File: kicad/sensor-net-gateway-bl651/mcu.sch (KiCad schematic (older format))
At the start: 14 parts

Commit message: added power and usb2uart
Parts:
- gave numbers to parts that had none: 14
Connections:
- net FTDI_DIO0: now reaches BL1.12 (P0.12)
- net FTDI_DIO1: now reaches BL1.13 (P0.11)
- net FTDI_DIO2: now reaches BL1.14 (P0.10)
- net FTDI_DIO3: now reaches BL1.15 (P0.09)
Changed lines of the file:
@@
 $EndDescr
 $Comp
-L HH_Laird:BL651 BL?
+L HH_Laird:BL651 BL1
 U 1 1 5F8C7148
 P 5700 2900
-F 0 "BL?" H 5700 3915 50  0000 C CNN
+F 0 "BL1" H 5700 3915 50  0000 C CNN
 F 1 "BL651" H 5700 3824 50  0000 C CNN
 F 2 "HH_Laird:BL651" V 4900 3300 50  0001 C CNN
@@
 $EndComp
 $Comp
-L power:GND #PWR?
+L power:GND #PWR0101
 U 1 1 5F8C844D
 P 7250 2250
-F 0 "#PWR?" H 7250 2000 50  0001 C CNN
+F 0 "#PWR0101" H 7250 2000 50  0001 C CNN
 F 1 "GND" H 7255 2077 50  0000 C CNN
 F 2 "" H 7250 2250 50  0001 C CNN
@@
 $EndComp
 $Comp
-L power:GND #PWR?
+L power:GND #PWR0102
 U 1 1 5F8C8B4E
 P 4100 2650
-F 0 "#PWR?" H 4100 2400 50  0001 C CNN
+F 0 "#PWR0102" H 4100 2400 50  0001 C CNN
 F 1 "GND" H 4105 2477 50  0000 C CNN
 F 2 "" H 4100 2650 50  0001 C CNN
@@
 $EndComp
 $Comp
-L power:GND #PWR?
+L power:GND #PWR0103
 U 1 1 5F8C8EC1
 P 4450 4650
-F 0 "#PWR?" H 4450 4400 50  0001 C CNN
+F 0 "#PWR0103" H 4450 4400 50  0001 C CNN
 F 1 "GND" H 4455 4477 50  0000 C CNN
 F 2 "" H 4450 4650 50  0001 C CNN
@@
 $EndComp
 $Comp
-L power:GND #PWR?
+L power:GND #PWR0104
 U 1 1 5F8C9CA6
 P 7250 3850
-F 0 "#PWR?" H 7250 3600 50  0001 C CNN
+F 0 "#PWR0104" H 7250 3600 50  0001 C CNN
 F 1 "GND" H 7255 3677 50  0000 C CNN
 F 2 "" H 7250 3850 50  0001 C CNN
@@
 VDD
 $Comp
-L Device:C C?
+L Device:C C14
 U 1 1 5F8CD181
 P 4850 4450
-F 0 "C?" V 4598 4450 50  0000 C CNN
+F 0 "C14" V 4598 4450 50  0000 C CNN
 F 1 "0.1µF,16V" V 4689 4450 50  0000 C CNN
 F 2 "" H 4888 4300 50  0001 C CNN
@@
 UART_RX
 $Comp
-L Device:Crystal Y?
+L Device:Crystal Y1
 U 1 1 5F8D8EC9
 P 5450 5200
-F 0 "Y?" H 5450 5468 50  0000 C CNN
+F 0 "Y1" H 5450 5468 50  0000 C CNN
 F 1 "32.768 kHz" H 5450 5377 50  0000 C CNN
 F 2 "Crystal:Crystal_SMD_MicroCrystal_CC7V-T1A-2Pin_3.2x1.5mm" H 5450 5200 50  0001 C CNN
@@
 	5200 4850 5400 4850
 $Comp
-L Device:C C?
+L Device:C C15
 U 1 1 5F8DE5D5
 P 5200 5500
-F 0 "C?" H 5315 5546 50  0000 L CNN
+F 0 "C15" H 5315 5546 50  0000 L CNN
 F 1 "9pF" H 5315 5455 50  0000 L CNN
 F 2 "" H 5238 5350 50  0001 C CNN
@@
 $EndComp
 $Comp
-L Device:C C?
+L Device:C C16
 U 1 1 5F8DEC89
 P 5700 5500
-F 0 "C?" H 5815 5546 50  0000 L CNN
+F 0 "C16" H 5815 5546 50  0000 L CNN
 F 1 "9pF" H 5815 5455 50  0000 L CNN
 F 2 "" H 5738 5350 50  0001 C CNN
@@
 Connection ~ 5700 5200
 $Comp
-L power:GND #PWR?
+L power:GND #PWR0105
 U 1 1 5F8DF9F6
 P 5450 5850
-F 0 "#PWR?" H 5450 5600 50  0001 C CNN
+F 0 "#PWR0105" H 5450 5600 50  0001 C CNN
 F 1 "GND" H 5455 5677 50  0000 C CNN
 F 2 "" H 5450 5850 50  0001 C CNN
@@
 Connection ~ 5450 5850
 $Comp
-L HH_ARM:CORTEX-DEBUG CD?
+L HH_ARM:CORTEX-DEBUG CD1
 U 1 1 5F8E0A93
 P 9450 2800
-F 0 "CD?" H 9450 3387 60  0000 C CNN
+F 0 "CD1" H 9450 3387 60  0000 C CNN
 F 1 "CORTEX-DEBUG" H 9450 3281 60  0000 C CNN
 F 2 "" H 9450 2800 60  0001 C CNN
@@
 $EndComp
 $Comp
-L power:GND #PWR?
+L power:GND #PWR0106
 U 1 1 5F8E1A6E
 P 8600 3250
-F 0 "#PWR?" H 8600 3000 50  0001 C CNN
+F 0 "#PWR0106" H 8600 3000 50  0001 C CNN
 F 1 "GND" H 8605 3077 50  0000 C CNN
 F 2 "" H 8600 3250 50  0001 C CNN
@@
 SWO
 $Comp
-L HH_CnK:PTS526_SM15_SMTR2_LFS SW?
+L HH_CnK:PTS526_SM15_SMTR2_LFS SW1
 U 1 1 5F8E9ABE
 P 2100 2400
-F 0 "SW?" H 2100 2685 50  0000 C CNN
+F 0 "SW1" H 2100 2685 50  0000 C CNN
 F 1 "PTS526_SM15_SMTR2_LFS" H 2100 2594 50  0000 C CNN
 F 2 "CnK:PTS526-SM15-SMTR2-LFS" H 2100 2600 50  0001 C CNN
@@
 $EndComp
 $Comp
-L Device:C C?
+L Device:C C13
 U 1 1 5F8EA168
 P 2100 2750
-F 0 "C?" V 1848 2750 50  0000 C CNN
+F 0 "C13" V 1848 2750 50  0000 C CNN
 F 1 "0.1µF,16V" V 1939 2750 50  0000 C CNN
 F 2 "" H 2138 2600 50  0001 C CNN
@@
 $EndComp
 $Comp
-L power:GND #PWR?
+L power:GND #PWR0107
 U 1 1 5F8EBB2F
 P 1500 2900
-F 0 "#PWR?" H 1500 2650 50  0001 C CNN
+F 0 "#PWR0107" H 1500 2650 50  0001 C CNN
 F 1 "GND" H 1505 2727 50  0000 C CNN
 F 2 "" H 1500 2900 50  0001 C CNN
@@
 Connection ~ 2650 2600
 $Comp
-L HH_Hochreiner:Sensor-Connector SC?
+L HH_Hochreiner:Sensor-Connector SC1
 U 1 1 5F903C86
 P 2300 4750
-F 0 "SC?" H 2300 5315 50  0000 C CNN
+F 0 "SC1" H 2300 5315 50  0000 C CNN
 F 1 "Sensor-Connector" H 2300 5224 50  0000 C CNN
 F 2 "HH_Hochreiner:Sensor-Connector_M50-3150542R" H 2300 4750 50  0001 C CNN
@@
 $EndComp
 $Comp
-L power:GND #PWR?
+L power:GND #PWR0108
 U 1 1 5F904E15
 P 1400 4400
-F 0 "#PWR?" H 1400 4150 50  0001 C CNN
+F 0 "#PWR0108" H 1400 4150 50  0001 C CNN
 F 1 "GND" H 1405 4227 50  0000 C CNN
 F 2 "" H 1400 4400 50  0001 C CNN
@@
 ~RESET
 $Comp
-L power:GND #PWR?
+L power:GND #PWR0109
 U 1 1 5F9167AA
 P 8950 4400
-F 0 "#PWR?" H 8950 4150 50  0001 C CNN
+F 0 "#PWR0109" H 8950 4150 50  0001 C CNN
 F 1 "GND" H 8955 4227 50  0000 C CNN
 F 2 "" H 8950 4400 50  0001 C CNN
@@
 UART_TX
 $Comp
-L power:GND #PWR?
+L power:GND #PWR0110
 U 1 1 5F91986A
 P 8800 5550
-F 0 "#PWR?" H 8800 5300 50  0001 C CNN
+F 0 "#PWR0110" H 8800 5300 50  0001 C CNN
 F 1 "GND" H 8805 5377 50  0000 C CNN
 F 2 "" H 8800 5550 50  0001 C CNN
@@
 UART_RTS
 $Comp
-L HH_Harwin:M50-3130545 M?
+L HH_Harwin:M50-3130545 M1
 U 1 1 5F920E82
 P 9650 4300
-F 0 "M?" H 9778 4346 50  0000 L CNN
+F 0 "M1" H 9778 4346 50  0000 L CNN
 F 1 "M50-3130545" H 9778 4255 50  0000 L CNN
 F 2 "HH_Harwin:M50-3130545" H 9650 3400 50  0001 C CNN
@@
 $EndComp
 $Comp
-L HH_Harwin:M50-3130545 M?
+L HH_Harwin:M50-3130545 M2
 U 1 1 5F9214B1
 P 9650 5450
-F 0 "M?" H 9778 5496 50  0000 L CNN
+F 0 "M2" H 9778 5496 50  0000 L CNN
 F 1 "M50-3130545" H 9778 5405 50  0000 L CNN
 F 2 "HH_Harwin:M50-3130545" H 9650 4550 50  0001 C CNN
@@
 $EndComp
 $Comp
-L HH_Kingbright:APBD3224LSURKCGKC LED?
+L HH_Kingbright:APBD3224LSURKCGKC LED1
 U 1 1 5F924480
 P 2500 6650
-F 0 "LED?" H 2500 7015 50  0000 C CNN
+F 0 "LED1" H 2500 7015 50  0000 C CNN
 F 1 "APBD3224LSURKCGKC" H 2500 6924 50  0000 C CNN
 F 2 "HH_Kingbright:APBD3224LSURKCGKC" H 2500 6650 50  0001 C CNN
@@
 $EndComp
 $Comp
-L Device:R R?
+L Device:R R3
 U 1 1 5F924FDE
 P 3800 6550
-F 0 "R?" V 3593 6550 50  0000 C CNN
+F 0 "R3" V 3593 6550 50  0000 C CNN
 F 1 "R" V 3684 6550 50  0000 C CNN
 F 2 "" V 3730 6550 50  0001 C CNN
@@
 $EndComp
 $Comp
-L Device:R R?
+L Device:R R4
 U 1 1 5F9257BE
 P 3800 6750
-F 0 "R?" V 3593 6750 50  0000 C CNN
+F 0 "R4" V 3593 6750 50  0000 C CNN
 F 1 "R" V 3684 6750 50  0000 C CNN
 F 2 "" V 3730 6750 50  0001 C CNN
@@
 $EndComp
 $Comp
-L power:GND #PWR?
+L power:GND #PWR0111
 U 1 1 5F9284BE
 P 1450 6900
-F 0 "#PWR?" H 1450 6650 50  0001 C CNN
+F 0 "#PWR0111" H 1450 6650 50  0001 C CNN
 F 1 "GND" H 1455 6727 50  0000 C CNN
 F 2 "" H 1450 6900 50  0001 C CNN
@@
 Text Notes 10050 2000 2    100  ~ 20
 Debug Connectors
+Text HLabel 6600 3250 2    50   Input ~ 0
+FTDI_DIO0
+Text HLabel 6600 3350 2    50   Input ~ 0
+FTDI_DIO1
+Text HLabel 6600 3450 2    50   Input ~ 0
+FTDI_DIO2
+Text HLabel 6600 3550 2    50   Input ~ 0
+FTDI_DIO3
 $EndSCHEMATC

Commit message: started layout
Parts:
- C13, C14, C15, C16: footprint (none) -> Capacitor_SMD:C_0603_1608Metric
- CD1: footprint (none) -> HH_CNCTech:CORTEX-DEBUG
- R3, R4: footprint (none) -> Resistor_SMD:R_0603_1608Metric
- SW1: footprint CnK:PTS526-SM15-SMTR2-LFS -> HH_CnK:PTS526-SM15-SMTR2-LFS
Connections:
- net SENSOR.SDA: now reaches BL1.29 (P0.15)
- net SENSOR.SCL: now reaches BL1.30 (P0.17)
- no-connect marks 0 -> 8
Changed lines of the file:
@@
 $Descr A4 11693 8268
 encoding utf-8
-Sheet 2 4
+Sheet 2 5
 Title ""
 Date ""
@@
 F 0 "C14" V 4598 4450 50  0000 C CNN
 F 1 "0.1µF,16V" V 4689 4450 50  0000 C CNN
-F 2 "" H 4888 4300 50  0001 C CNN
+F 2 "Capacitor_SMD:C_0603_1608Metric" H 4888 4300 50  0001 C CNN
 F 3 "~" H 4850 4450 50  0001 C CNN
 	1    4850 4450
@@
 F 0 "C15" H 5315 5546 50  0000 L CNN
 F 1 "9pF" H 5315 5455 50  0000 L CNN
-F 2 "" H 5238 5350 50  0001 C CNN
+F 2 "Capacitor_SMD:C_0603_1608Metric" H 5238 5350 50  0001 C CNN
 F 3 "~" H 5200 5500 50  0001 C CNN
 	1    5200 5500
@@
 F 0 "C16" H 5815 5546 50  0000 L CNN
 F 1 "9pF" H 5815 5455 50  0000 L CNN
-F 2 "" H 5738 5350 50  0001 C CNN
+F 2 "Capacitor_SMD:C_0603_1608Metric" H 5738 5350 50  0001 C CNN
 F 3 "~" H 5700 5500 50  0001 C CNN
 	1    5700 5500
@@
 F 0 "CD1" H 9450 3387 60  0000 C CNN
 F 1 "CORTEX-DEBUG" H 9450 3281 60  0000 C CNN
-F 2 "" H 9450 2800 60  0001 C CNN
+F 2 "HH_CNCTech:CORTEX-DEBUG" H 9450 2800 60  0001 C CNN
 F 3 "" H 9450 2800 60  0001 C CNN
 	1    9450 2800
@@
 F 0 "SW1" H 2100 2685 50  0000 C CNN
 F 1 "PTS526_SM15_SMTR2_LFS" H 2100 2594 50  0000 C CNN
-F 2 "CnK:PTS526-SM15-SMTR2-LFS" H 2100 2600 50  0001 C CNN
+F 2 "HH_CnK:PTS526-SM15-SMTR2-LFS" H 2100 2600 50  0001 C CNN
 F 3 "https://dznh3ojzb2azq.cloudfront.net/products/Tactile/PTS526/documents/datasheet.pdf" H 2100 2600 50  0001 C CNN
 F 4 "CKN12220-1-ND" H 2100 2400 50  0001 C CNN "Digi-Key Part Number"
@@
 F 0 "C13" V 1848 2750 50  0000 C CNN
 F 1 "0.1µF,16V" V 1939 2750 50  0000 C CNN
-F 2 "" H 2138 2600 50  0001 C CNN
+F 2 "Capacitor_SMD:C_0603_1608Metric" H 2138 2600 50  0001 C CNN
 F 3 "~" H 2100 2750 50  0001 C CNN
 	1    2100 2750
@@
 F 0 "R3" V 3593 6550 50  0000 C CNN
 F 1 "R" V 3684 6550 50  0000 C CNN
-F 2 "" V 3730 6550 50  0001 C CNN
+F 2 "Resistor_SMD:R_0603_1608Metric" V 3730 6550 50  0001 C CNN
 F 3 "~" H 3800 6550 50  0001 C CNN
 	1    3800 6550
@@
 F 0 "R4" V 3593 6750 50  0000 C CNN
 F 1 "R" V 3684 6750 50  0000 C CNN
-F 2 "" V 3730 6750 50  0001 C CNN
+F 2 "Resistor_SMD:R_0603_1608Metric" V 3730 6750 50  0001 C CNN
 F 3 "~" H 3800 6750 50  0001 C CNN
 	1    3800 6750
@@
 Text HLabel 6600 3550 2    50   Input ~ 0
 FTDI_DIO3
+Text HLabel 4800 3450 0    50   Input ~ 0
+SENSOR.SCL
+Text HLabel 4800 3550 0    50   Input ~ 0
+SENSOR.SDA
+NoConn ~ 6600 3150
+NoConn ~ 6600 3050
+NoConn ~ 6600 2850
+NoConn ~ 6600 2450
+NoConn ~ 5600 4050
+NoConn ~ 5700 4050
+NoConn ~ 5800 4050
+NoConn ~ 4800 3650
 $EndSCHEMATC

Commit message: routing snapshot
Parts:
- removed CD1: CORTEX-DEBUG, HH_CNCTech:CORTEX-DEBUG, symbol HH_ARM:CORTEX-DEBUG
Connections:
- net FTDI_DIO0: now also BL1.13 (P0.11); no longer BL1.12 (P0.12)
- net FTDI_DIO1: now also BL1.12 (P0.12); no longer BL1.13 (P0.11)
- net FTDI_DIO2: now also BL1.15 (P0.09); no longer BL1.14 (P0.10)
- net FTDI_DIO3: now also BL1.14 (P0.10); no longer BL1.15 (P0.09)
- net GPIO_1: now also BL1.37 (P0.26); no longer BL1.34 (P0.29)
- net GPIO_2: now also BL1.30 (P0.17); no longer BL1.33 (P0.30)
- net I2C_SDA: now also BL1.35 (P0.28); no longer BL1.37 (P0.26)
- net LED_GREEN: now also BL1.2 (P0.24); no longer BL1.31 (P0.19)
- net LED_RED: now also BL1.3 (P0.23); no longer BL1.32 (P0.31)
- net SENSOR.SCL: now also BL1.28 (P0.13); no longer BL1.30 (P0.17)
- net SPI_CLK: now also BL1.32 (P0.31); no longer BL1.38 (P0.25)
- net SPI_MISO: now also BL1.34 (P0.29); no longer BL1.2 (P0.24)
- net SPI_MOSI: now also BL1.33 (P0.30); no longer BL1.3 (P0.23)
- net SWO: now also M2.2
- net UART_CTS: no longer M2.4
- net UART_RTS: no longer M2.5
- net UART_RX: no longer M2.2
- net UART_TX: no longer M2.1
- net VDD: now also M2.1
- net ~SPI_CS: now also BL1.31 (P0.19); no longer BL1.35 (P0.28)
- net UART2.TX: now reaches BL1.21 (P0.04)
- net UART2.TX: now also M2.4
- net UART2.RX: now reaches BL1.22 (P0.03)
- net UART2.RX: now also M2.5
- no-connect marks 8 -> 6
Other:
- moved on the sheet: M1, M2
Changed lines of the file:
@@
 U 1 1 5F8C7148
 P 5700 2900
+AR Path="/5F8C7148" Ref="BL1"  Part="1"
+AR Path="/5F8C705B/5F8C7148" Ref="BL1"  Part="1"
 F 0 "BL1" H 5700 3915 50  0000 C CNN
 F 1 "BL651" H 5700 3824 50  0000 C CNN
@@
 	0    1    1    0
 $EndComp
-Text Label 6600 2950 0    50   ~ 0
-SWO
 Text Label 6600 2750 0    50   ~ 0
 ~RESET
@@
 Text Label 6600 2550 0    50   ~ 0
 SWDIO
-Text Label 4800 2650 2    50   ~ 0
+Text Label 4800 3250 2    50   ~ 0
 SPI_CLK
-Text Label 4800 2750 2    50   ~ 0
+Text Label 4800 2950 2    50   ~ 0
 I2C_SDA
 Text Label 4800 2850 2    50   ~ 0
 I2C_SCL
-Text Label 6600 2250 0    50   ~ 0
+Text Label 4800 3050 2    50   ~ 0
 SPI_MISO
-Text Label 6600 2350 0    50   ~ 0
+Text Label 4800 3150 2    50   ~ 0
 SPI_MOSI
 Wire Wire Line
@@
 	5700 5850 5700 5650
 Connection ~ 5450 5850
-$Comp
-L HH_ARM:CORTEX-DEBUG CD1
-U 1 1 5F8E0A93
-P 9450 2800
-F 0 "CD1" H 9450 3387 60  0000 C CNN
-F 1 "CORTEX-DEBUG" H 9450 3281 60  0000 C CNN
-F 2 "HH_CNCTech:CORTEX-DEBUG" H 9450 2800 60  0001 C CNN
-F 3 "" H 9450 2800 60  0001 C CNN
-	1    9450 2800
-	1    0    0    -1
-$EndComp
-$Comp
-L power:GND #PWR0106
-U 1 1 5F8E1A6E
-P 8600 3250
-F 0 "#PWR0106" H 8600 3000 50  0001 C CNN
-F 1 "GND" H 8605 3077 50  0000 C CNN
-F 2 "" H 8600 3250 50  0001 C CNN
-F 3 "" H 8600 3250 50  0001 C CNN
-	1    8600 3250
-	1    0    0    -1
-$EndComp
-Wire Wire Line
-	8800 2700 8600 2700
-Wire Wire Line
-	8600 2700 8600 2800
-Wire Wire Line
-	8800 3000 8600 3000
-Connection ~ 8600 3000
-Wire Wire Line
-	8600 3000 8600 3250
-Wire Wire Line
-	8800 2800 8600 2800
-Connection ~ 8600 2800
-Wire Wire Line
-	8600 2800 8600 3000
-Text HLabel 8800 2600 0    50   Input ~ 0
-VDD
-Text Label 10100 2600 0    50   ~ 0
-SWDIO
-Text Label 10100 2700 0    50   ~ 0
-SWDCLK
-Text Label 10100 3000 0    50   ~ 0
-~RESET
-Text Label 10100 2800 0    50   ~ 0
-SWO
 $Comp
 L HH_CnK:PTS526_SM15_SMTR2_LFS SW1
@@
 Text Label 1650 4950 2    50   ~ 0
 GPIO_1
-Text Label 4800 2950 2    50   ~ 0
+Text Label 4800 3350 2    50   ~ 0
 ~SPI_CS
-Text Label 4800 3150 2    50   ~ 0
+Text Label 4800 3450 2    50   ~ 0
 GPIO_2
-Text Label 4800 3050 2    50   ~ 0
+Text Label 4800 2750 2    50   ~ 0
 GPIO_1
-Text HLabel 9350 4100 0    50   Input ~ 0
+Text HLabel 9200 2500 0    50   Input ~ 0
 VDD
-Text Label 9350 4200 2    50   ~ 0
+Text Label 9200 2600 2    50   ~ 0
 ~RESET
 $Comp
 L power:GND #PWR0109
 U 1 1 5F9167AA
-P 8950 4400
-F 0 "#PWR0109" H 8950 4150 50  0001 C CNN
-F 1 "GND" H 8955 4227 50  0000 C CNN
-F 2 "" H 8950 4400 50  0001 C CNN
-F 3 "" H 8950 4400 50  0001 C CNN
-	1    8950 4400
-	1    0    0    -1
-$EndComp
-Wire Wire Line
-	8950 4400 8950 4300
-Wire Wire Line
-	8950 4300 9350 4300
-Text Label 9350 4400 2    50   ~ 0
+P 8800 2800
+F 0 "#PWR0109" H 8800 2550 50  0001 C CNN
+F 1 "GND" H 8805 2627 50  0000 C CNN
+F 2 "" H 8800 2800 50  0001 C CNN
+F 3 "" H 8800 2800 50  0001 C CNN
+	1    8800 2800
+	1    0    0    -1
+$EndComp
+Wire Wire Line
+	8800 2800 8800 2700
+Wire Wire Line
+	8800 2700 9200 2700
+Text Label 9200 2800 2    50   ~ 0
 SWDCLK
-Text Label 9350 4500 2    50   ~ 0
+Text Label 9200 2900 2    50   ~ 0
 SWDIO
-Text HLabel 9350 5350 0    50   Input ~ 0
-UART_RX
-Text HLabel 9350 5250 0    50   Input ~ 0
-UART_TX
 $Comp
 L power:GND #PWR0110
 U 1 1 5F91986A
-P 8800 5550
-F 0 "#PWR0110" H 8800 5300 50  0001 C CNN
-F 1 "GND" H 8805 5377 50  0000 C CNN
-F 2 "" H 8800 5550 50  0001 C CNN
-F 3 "" H 8800 5550 50  0001 C CNN
-	1    8800 5550
-	1    0    0    -1
-$EndComp
-Wire Wire Line
-	8800 5550 8800 5450
-Wire Wire Line
-	8800 5450 9350 5450
-Text HLabel 9350 5550 0    50   Input ~ 0
-UART_CTS
-Text HLabel 9350 5650 0    50   Input ~ 0
-UART_RTS
+P 8650 3950
+F 0 "#PWR0110" H 8650 3700 50  0001 C CNN
+F 1 "GND" H 8655 3777 50  0000 C CNN
+F 2 "" H 8650 3950 50  0001 C CNN
+F 3 "" H 8650 3950 50  0001 C CNN
+	1    8650 3950
+	1    0    0    -1
+$EndComp
+Wire Wire Line
+	8650 3950 8650 3850
+Wire Wire Line
+	8650 3850 9200 3850
 $Comp
 L HH_Harwin:M50-3130545 M1
 U 1 1 5F920E82
-P 9650 4300
-F 0 "M1" H 9778 4346 50  0000 L CNN
-F 1 "M50-3130545" H 9778 4255 50  0000 L CNN
-F 2 "HH_Harwin:M50-3130545" H 9650 3400 50  0001 C CNN
-F 3 "https://cdn.harwin.com/pdfs/M50-313.pdf" H 9650 3500 50  0001 C CNN
-F 4 "952-3585-ND" H 9650 3800 50  0001 C CNN "DigiKey_PartNumber"
-F 5 "Harwin Inc." H 9650 3700 50  0001 C CNN "Manufacturer"
-F 6 "M50-3130545" H 9650 3600 50  0001 C CNN "Manufacturer_PartNumber"
-	1    9650 4300
+P 9500 2700
+F 0 "M1" H 9628 2746 50  0000 L CNN
+F 1 "M50-3130545" H 9628 2655 50  0000 L CNN
+F 2 "HH_Harwin:M50-3130545" H 9500 1800 50  0001 C CNN
+F 3 "https://cdn.harwin.com/pdfs/M50-313.pdf" H 9500 1900 50  0001 C CNN
+F 4 "952-3585-ND" H 9500 2200 50  0001 C CNN "DigiKey_PartNumber"
+F 5 "Harwin Inc." H 9500 2100 50  0001 C CNN "Manufacturer"
+F 6 "M50-3130545" H 9500 2000 50  0001 C CNN "Manufacturer_PartNumber"
+	1    9500 2700
 	1    0    0    -1
 $EndComp
@@
 L HH_Harwin:M50-3130545 M2
 U 1 1 5F9214B1
-P 9650 5450
-F 0 "M2" H 9778 5496 50  0000 L CNN
-F 1 "M50-3130545" H 9778 5405 50  0000 L CNN
-F 2 "HH_Harwin:M50-3130545" H 9650 4550 50  0001 C CNN
-F 3 "https://cdn.harwin.com/pdfs/M50-313.pdf" H 9650 4650 50  0001 C CNN
-F 4 "952-3585-ND" H 9650 4950 50  0001 C CNN "DigiKey_PartNumber"
-F 5 "Harwin Inc." H 9650 4850 50  0001 C CNN "Manufacturer"
-F 6 "M50-3130545" H 9650 4750 50  0001 C CNN "Manufacturer_PartNumber"
-	1    9650 5450
+P 9500 3850
+F 0 "M2" H 9628 3896 50  0000 L CNN
+F 1 "M50-3130545" H 9628 3805 50  0000 L CNN
+F 2 "HH_Harwin:M50-3130545" H 9500 2950 50  0001 C CNN
+F 3 "https://cdn.harwin.com/pdfs/M50-313.pdf" H 9500 3050 50  0001 C CNN
+F 4 "952-3585-ND" H 9500 3350 50  0001 C CNN "DigiKey_PartNumber"
+F 5 "Harwin Inc." H 9500 3250 50  0001 C CNN "Manufacturer"
+F 6 "M50-3130545" H 9500 3150 50  0001 C CNN "Manufacturer_PartNumber"
+	1    9500 3850
 	1    0    0    -1
 $EndComp
@@
 Text Label 3950 6750 0    50   ~ 0
 LED_GREEN
-Text Label 4800 3350 2    50   ~ 0
+Text Label 6600 2250 0    50   ~ 0
 LED_GREEN
-Text Label 4800 3250 2    50   ~ 0
+Text Label 6600 2350 0    50   ~ 0
 LED_RED
 Text Notes 3050 6050 2    100  ~ 20
@@
 Text Notes 10050 2000 2    100  ~ 20
 Debug Connectors
+Text HLabel 6600 3350 2    50   Input ~ 0
+FTDI_DIO0
 Text HLabel 6600 3250 2    50   Input ~ 0
-FTDI_DIO0
-Text HLabel 6600 3350 2    50   Input ~ 0
 FTDI_DIO1
+Text HLabel 6600 3550 2    50   Input ~ 0
+FTDI_DIO2
 Text HLabel 6600 3450 2    50   Input ~ 0
-FTDI_DIO2
-Text HLabel 6600 3550 2    50   Input ~ 0
 FTDI_DIO3
-Text HLabel 4800 3450 0    50   Input ~ 0
+Text HLabel 4800 3650 0    50   Input ~ 0
 SENSOR.SCL
 Text HLabel 4800 3550 0    50   Input ~ 0
@@
 NoConn ~ 6600 2450
 NoConn ~ 5600 4050
-NoConn ~ 5700 4050
-NoConn ~ 5800 4050
-NoConn ~ 4800 3650
+NoConn ~ 4800 2650
+Text HLabel 9200 3650 0    50   Input ~ 0
+VDD
+Text Label 6600 2950 0    50   ~ 0
+SWO
+Text Label 5700 4050 3    50   ~ 0
+UART2.RX
+Text Label 5800 4050 3    50   ~ 0
+UART2.TX
+Text Label 9200 3750 2    50   ~ 0
+SWO
+Text Label 9200 4050 2    50   ~ 0
+UART2.RX
+Text Label 9200 3950 2    50   ~ 0
+UART2.TX
 $EndSCHEMATC

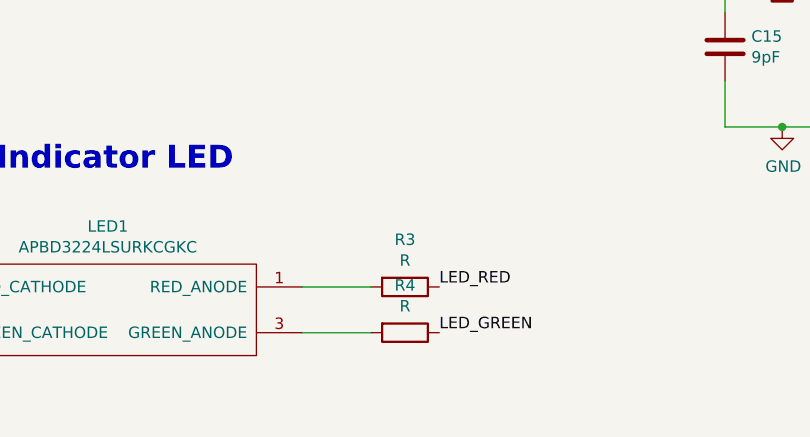
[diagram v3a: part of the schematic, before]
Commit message: added pin descriptions
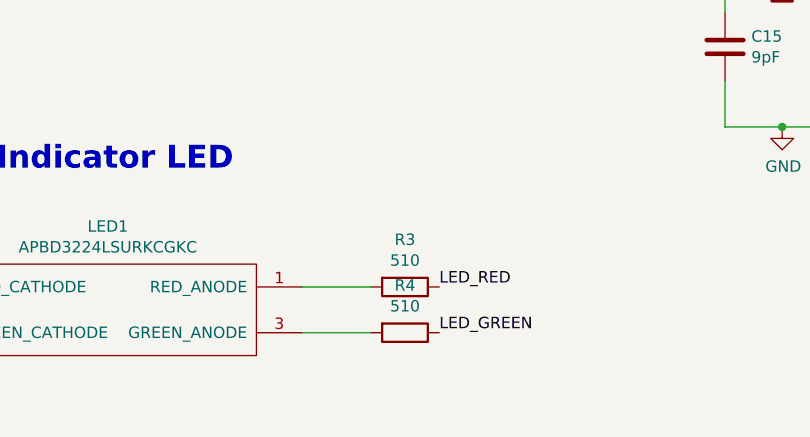
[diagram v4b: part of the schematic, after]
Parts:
- C15, C16: Description (none) -> CAP CER 9PF 50V NPO 0603; Digi-Key Part Number (none) -> 311-3866-1-ND; Manufacturer (none) -> Yageo; Manufacturer Part Number (none) -> CC0603CRNPO9BN9R0
- R3, R4: value R -> 510; Description (none) -> RES SMD 510 OHM 0.5% 1/16W 0603; Digi-Key Part Number (none) -> RR08P510DCT-ND; Manufacturer (none) -> Susumu; Manufacturer Part Number (none) -> RR0816P-511-D
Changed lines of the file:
@@
 F 1 "9pF" H 5315 5455 50  0000 L CNN
 F 2 "Capacitor_SMD:C_0603_1608Metric" H 5238 5350 50  0001 C CNN
-F 3 "~" H 5200 5500 50  0001 C CNN
+F 3 "https://www.yageo.com/upload/media/product/productsearch/datasheet/mlcc/UPY-GP_NP0_16V-to-50V_18.pdf" H 5200 5500 50  0001 C CNN
+F 4 "311-3866-1-ND" H 5200 5500 50  0001 C CNN "Digi-Key Part Number"
+F 5 "Yageo" H 5200 5500 50  0001 C CNN "Manufacturer"
+F 6 "CC0603CRNPO9BN9R0" H 5200 5500 50  0001 C CNN "Manufacturer Part Number"
+F 7 "CAP CER 9PF 50V NPO 0603" H 5200 5500 50  0001 C CNN "Description"
 	1    5200 5500
 	1    0    0    -1
@@
 F 1 "9pF" H 5815 5455 50  0000 L CNN
 F 2 "Capacitor_SMD:C_0603_1608Metric" H 5738 5350 50  0001 C CNN
-F 3 "~" H 5700 5500 50  0001 C CNN
+F 3 "https://www.yageo.com/upload/media/product/productsearch/datasheet/mlcc/UPY-GP_NP0_16V-to-50V_18.pdf" H 5700 5500 50  0001 C CNN
+F 4 "311-3866-1-ND" H 5700 5500 50  0001 C CNN "Digi-Key Part Number"
+F 5 "Yageo" H 5700 5500 50  0001 C CNN "Manufacturer"
+F 6 "CC0603CRNPO9BN9R0" H 5700 5500 50  0001 C CNN "Manufacturer Part Number"
+F 7 "CAP CER 9PF 50V NPO 0603" H 5700 5500 50  0001 C CNN "Description"
 	1    5700 5500
 	1    0    0    -1
@@
 P 3800 6550
 F 0 "R3" V 3593 6550 50  0000 C CNN
-F 1 "R" V 3684 6550 50  0000 C CNN
+F 1 "510" V 3684 6550 50  0000 C CNN
 F 2 "Resistor_SMD:R_0603_1608Metric" V 3730 6550 50  0001 C CNN
 F 3 "~" H 3800 6550 50  0001 C CNN
+F 4 "RR08P510DCT-ND" V 3800 6550 50  0001 C CNN "Digi-Key Part Number"
+F 5 "Susumu" V 3800 6550 50  0001 C CNN "Manufacturer"
+F 6 "RR0816P-511-D" V 3800 6550 50  0001 C CNN "Manufacturer Part Number"
+F 7 "RES SMD 510 OHM 0.5% 1/16W 0603" V 3800 6550 50  0001 C CNN "Description"
 	1    3800 6550
 	0    1    1    0
@@
 P 3800 6750
 F 0 "R4" V 3593 6750 50  0000 C CNN
-F 1 "R" V 3684 6750 50  0000 C CNN
+F 1 "510" V 3684 6750 50  0000 C CNN
 F 2 "Resistor_SMD:R_0603_1608Metric" V 3730 6750 50  0001 C CNN
 F 3 "~" H 3800 6750 50  0001 C CNN
+F 4 "RR08P510DCT-ND" V 3800 6750 50  0001 C CNN "Digi-Key Part Number"
+F 5 "Susumu" V 3800 6750 50  0001 C CNN "Manufacturer"
+F 6 "RR0816P-511-D" V 3800 6750 50  0001 C CNN "Manufacturer Part Number"
+F 7 "RES SMD 510 OHM 0.5% 1/16W 0603" V 3800 6750 50  0001 C CNN "Description"
 	1    3800 6750
 	0    1    1    0
